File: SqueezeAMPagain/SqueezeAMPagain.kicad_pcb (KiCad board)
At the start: 2 copper layers, 100.5 x 104 mm, 183 parts, among them J1 Conn_01x02_Pin, J10 Conn_02x07_Odd_Even, J2 Conn_01x02_Pin, J3 Raspberry_Pi_2_3, J4 Conn_01x06_Pin, J5 USB_B_Micro, J6 Conn_01x02_Pin, J7 Barrel_Jack_Switch_MountingPin, J8 Conn_02x08_Odd_Even, J9 Conn_01x06_Pin, Q1 Q_NPN_BEC, Q10 AO3401A, Q3 AO3401A, Q4 Q_NPN_BEC, Q5 Q_NPN_BEC, Q6 Q_NPN_BEC, Q7 AO3401A, Q8 AO3401A, Q9 AO3401A, U1 TAS5756M, U2 RaspberryPi_Pico_W, U3 CP2102N-Axx-xQFN28, U4 ESP32-WROVER-E, U5 TPS5430DDA, U6 TSOP21xx, U7 AMS1117-3.3

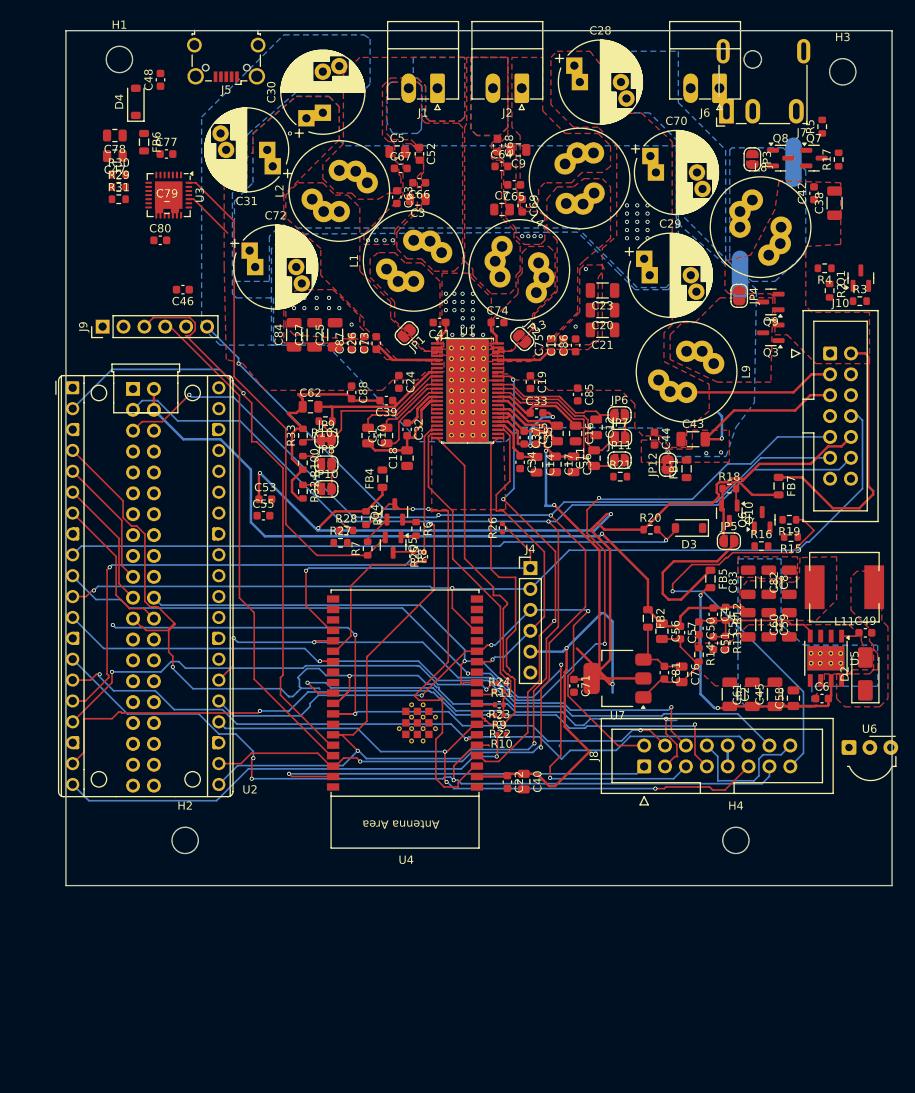
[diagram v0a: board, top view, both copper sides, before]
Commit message: Update SqueezeAMPagain.kicad_pcb, SqueezeAMPagain.kicad_prl, SqueezeAMPagain.kicad_pro, and 5 more files
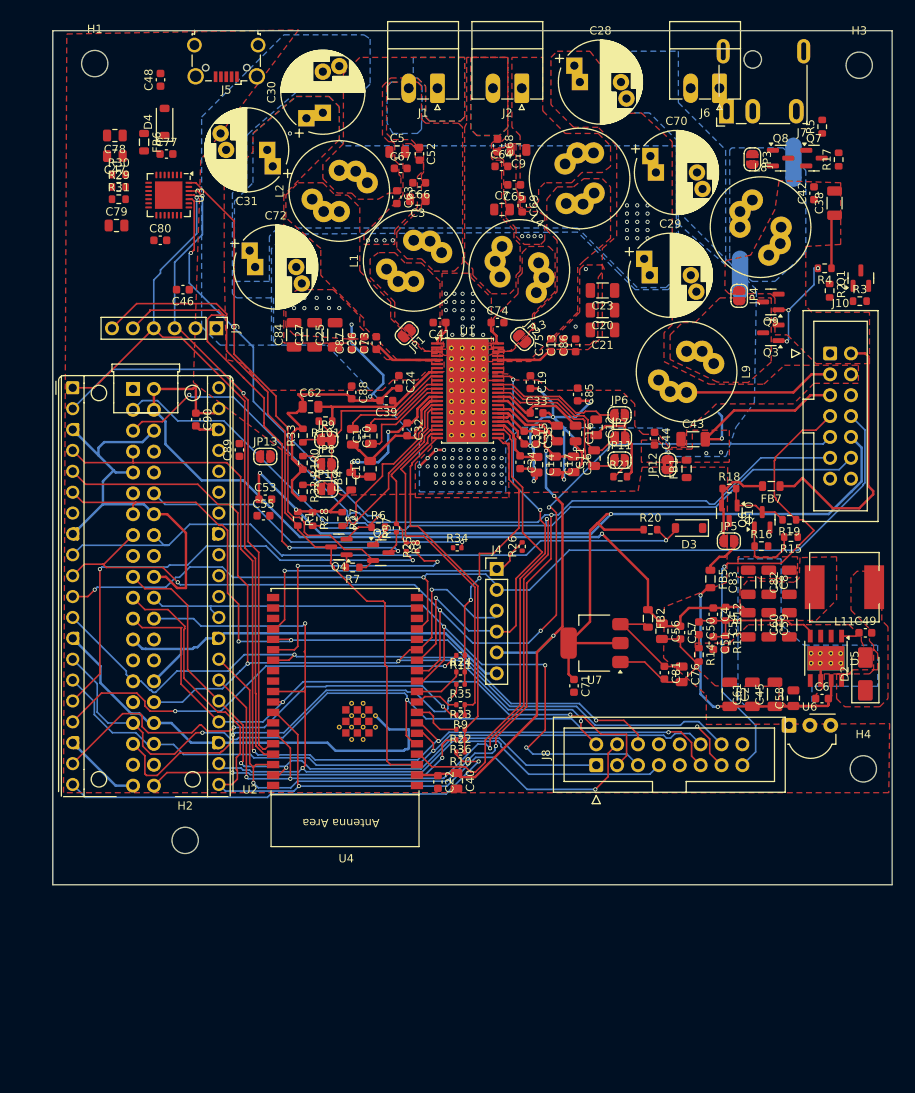
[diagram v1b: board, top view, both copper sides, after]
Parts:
- added C89: 100n, Capacitor_SMD:C_0603_1608Metric, F.Cu at (85.1, 71.0)
- added C90: 100n, Capacitor_SMD:C_0603_1608Metric, F.Cu at (79.8, 67.3)
- added JP13: LV On, Jumper:SolderJumper-2_P1.3mm_Open_RoundedPad1.0x1.5mm, F.Cu at (88.2, 71.8)
- added R34: 33, Resistor_SMD:R_0402_1005Metric, F.Cu at (111.6, 82.9)
- added R35: 33, Resistor_SMD:R_0402_1005Metric, F.Cu at (112.0, 99.5)
- added R36: 33, Resistor_SMD:R_0402_1005Metric, F.Cu at (112.0, 106.2)
- added R37: 33, Resistor_SMD:R_0402_1005Metric, F.Cu at (104.2, 80.5)
- U2: footprint pipico:RaspberryPi_Pico_Common_THT -> pipico_reduced:RaspberryPi_Pico_Common_THT_nokeepout
- moved H4 17.8 mm to (161.0, 109.8)
- moved J9 13.8 mm to (82.3, 56.2), turned to -90 degrees
- moved C22 8.45 mm to (109.2, 111.4)
- moved R1 8.30 mm to (92.2, 79.4)
- moved C40 8.20 mm to (111.5, 111.2)
- moved Q4 8.03 mm to (97.2, 82.8), turned to 180 degrees
- moved U6 7.78 mm to (152.0, 104.5)
- moved U4 7.30 mm to (98.0, 103.6)
- moved C79 6.53 mm to (70.2, 43.7)
- moved R11 6.05 mm to (112.0, 96.0)
- moved J8 5.83 mm to (128.5, 109.4)
- moved R10 5.44 mm to (112.0, 107.8)
- moved R24 5.29 mm to (112.0, 98.0)
- moved U7 5.13 mm to (128.3, 94.5)
- moved R22 4.84 mm to (112.0, 105.0)
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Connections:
- D3 pad 2: /Pico/GPIO6 -> /Pi/GPIO23
- J10 pad 9: /Pico/GPIO7 -> /Pi/GPIO22
- J3 pad 12: /Amp/SCLK -> Net-(J3-GPIO18/PWM0)
- J3 pad 13: unconnected-(J3-GPIO27-Pad13) -> /FPConnector/RESET
- J3 pad 15: unconnected-(J3-GPIO22-Pad15) -> /Pi/GPIO22
- J3 pad 16: unconnected-(J3-GPIO23-Pad16) -> /Pi/GPIO23
- J3 pad 18: unconnected-(J3-GPIO24-Pad18) -> /esp/TCK
- J3 pad 29: unconnected-(J3-GCLK1/GPIO5-Pad29) -> /FPConnector/IO4
- J3 pad 32: /Pi/PWM -> /esp/TDI
- J3 pad 33: unconnected-(J3-PWM1/GPIO13-Pad33) -> /FPConnector/IO3
- J3 pad 35: /Amp/LRCLK/FS -> Net-(J3-GPIO19/MISO1)
- J3 pad 36: unconnected-(J3-GPIO16-Pad36) -> /FPConnector/IO2
- J3 pad 40: /Amp/SDIN -> Net-(J3-GPIO21/SCLK1)
- J3 pad 7: unconnected-(J3-GCLK0/GPIO4-Pad7) -> /FPConnector/IO1
- R2 pad 1: /Pico/GPIO7 -> /Pi/GPIO22
- R20 pad 2: /Pico/GPIO6 -> /Pi/GPIO23
- R25 pad 2: /USB-Uart/BOOT -> /Amp/MCLK
- R26 pad 1: /Pico/GPIO6 -> /Pi/GPIO23
- R8 pad 1: /USB-Uart/BOOT -> /Amp/MCLK
- U1 pad 22: /USB-Uart/BOOT -> /Amp/MCLK
- U2 pad 10: /Pico/GPIO7 -> /Pi/GPIO22
- U2 pad 21: /SDA -> /FPConnector/MISO
- U2 pad 22: /SCL -> /FPConnector/CS
- U2 pad 24: /FPConnector/IO1 -> /FPConnector/SCK
- U2 pad 25: /esp/TDI -> /FPConnector/MOSI
- U2 pad 26: /FPConnector/RESET -> /SDA
- U2 pad 27: unconnected-(U2-GPIO21-Pad27) -> /SCL
- U2 pad 29: unconnected-(U2-GPIO22-Pad29) -> /FPConnector/D/C
- U2 pad 36: unconnected-(U2-3V3-Pad36) -> Net-(JP13-A)
- U2 pad 39: unconnected-(U2-VSYS-Pad39) -> +5V
- U2 pad 4: /FPConnector/SCK -> /FPConnector/IO1
- U2 pad 5: /FPConnector/MOSI -> /esp/TDI
- U2 pad 6: /FPConnector/MISO -> /FPConnector/RESET
- U2 pad 7: /FPConnector/CS -> unconnected-(U2-GPIO5-Pad7)
- U2 pad 9: /Pico/GPIO6 -> /Pi/GPIO23
- U4 pad 12: /Pico/GPIO7 -> /Pi/GPIO22
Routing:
- net GND: track 31.9 -> 191.5 mm
- net /Pi/GPIO22: track 0.00 -> 130.7 mm, vias 0 -> 4
- net /Pico/GPIO7: track 125.2 -> 0.00 mm, vias 3 -> 0
- net /Pi/GPIO23: track 0.00 -> 82.1 mm, vias 0 -> 1
- net /Pico/GPIO6: track 76.6 -> 0.00 mm, vias 1 -> 0
- net PGND: track 84.9 -> 156.7 mm, vias 46 -> 99
- net Net-(Q4-E): track 8.19 -> 60.1 mm, vias 0 -> 3
- net Net-(J3-GPIO19/MISO1): track 0.00 -> 50.5 mm, vias 0 -> 2
- net /esp/TDI: track 74.4 -> 123.3 mm, vias 3 -> 4
- net /FPConnector/SCK: track 123.7 -> 79.5 mm, vias 3 -> 2
- net /USB-Uart/BOOT: track 19.9 -> 64.0 mm, vias 0 -> 2
- net /FPConnector/IO1: track 76.6 -> 119.5 mm
- net Net-(J3-GPIO18/PWM0): track 0.00 -> 40.7 mm, vias 0 -> 1
- net Net-(J3-GPIO21/SCLK1): track 0.00 -> 40.3 mm, vias 0 -> 2
- net /SCL: track 170.2 -> 201.2 mm, vias 6 -> 5
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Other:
- board size 100.5 x 104 mm -> 102.1 x 103.9 mm

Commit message: Update SqueezeAMPagain.kicad_pcb, SqueezeAMPagain.kicad_prl, SqueezeAMPagain.kicad_pro, and 5 more files
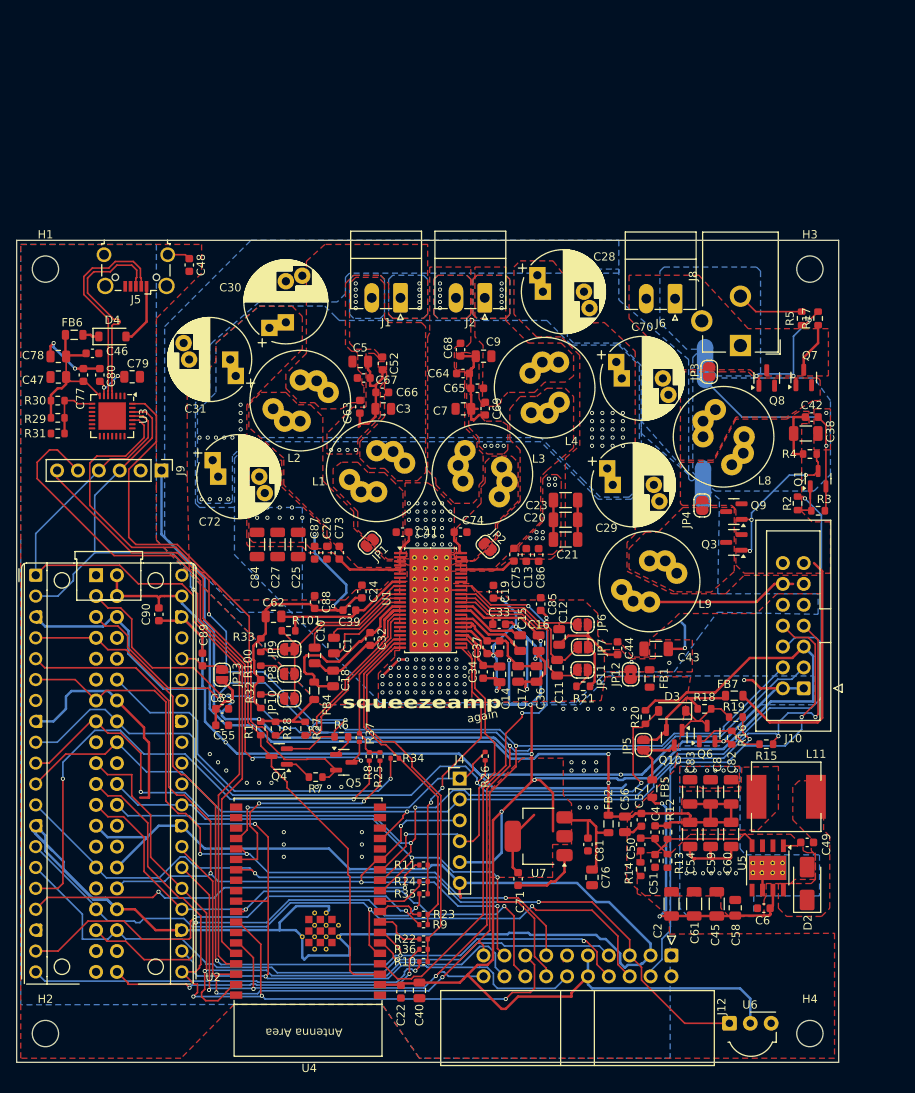
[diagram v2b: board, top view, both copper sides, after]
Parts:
- removed J7: Barrel_Jack_Switch_MountingPin, Connector_BarrelJack:BarrelJack_CUI_PJ-079BH_Horizontal
- added J12: Conn_02x10_Odd_Even, Connector_IDC:IDC-Header_2x10_P2.54mm_Horizontal, F.Cu at (137.7, 132.5)
- J8: value Conn_02x08_Odd_Even -> Barrel_Jack_Switch; footprint Connector_IDC:IDC-Header_2x08_P2.54mm_Vertical -> Connector_BarrelJack:BarrelJack_CUI_PJ-102AH_Horizontal
- moved J8 54.0 mm to (146.1, 58.3), turned to 180 degrees
- moved J10 40.9 mm to (153.8, 100.0), turned to 180 degrees
- moved U6 37.0 mm to (144.7, 140.8)
- moved H4 32.8 mm to (154.5, 142.0)
- moved R31 29.5 mm to (63.0, 69.0)
- moved R29 29.1 mm to (63.0, 67.1)
- moved H2 29.0 mm to (61.5, 142.0)
- moved C77 28.7 mm to (66.1, 61.9), turned to 90 degrees
- moved R30 28.5 mm to (63.0, 65.0)
- moved C38 28.2 mm to (154.0, 69.0), turned to 0 degrees
- moved Q10 28.1 mm to (138.0, 106.0)
- moved J5 27.8 mm to (72.5, 49.2)
- moved C47 27.7 mm to (63.1, 62.1)
- moved C78 27.7 mm to (63.1, 59.6)
- moved U3 27.7 mm to (69.6, 66.9)
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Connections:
- J10 pad 1: V_{IN} -> GND
- J10 pad 10: +3.3V -> PGND
- J10 pad 11: /SCL -> PVDD
- J10 pad 12: /SDA -> PVDD
- J10 pad 13: GND -> V_{IN}
- J10 pad 14: GND -> V_{IN}
- J10 pad 2: V_{IN} -> GND
- J10 pad 3: PVDD -> /SDA
- J10 pad 4: PVDD -> /SCL
- J10 pad 5: PGND -> +3.3V
- J10 pad 6: PGND -> /Pi/GPIO22
- J10 pad 7: /FPConnector/~{WAKE} -> /esp/TCK
- J10 pad 8: /esp/TCK -> /FPConnector/~{WAKE}
- J10 pad 9: /Pi/GPIO22 -> PGND
- J3 pad 17: Net-(J3-3V3-Pad1) -> pipin17
- J5 pad 6: Net-(J5-Shield) -> 6nc1
- J6 pad 1: Net-(J6-Pin_1) -> /Power/GND_{supply}
- J6 pad 2: /Power/V_{supply} -> /Power/V_{supply,plug}
- J8 pad 1: /FPConnector/MOSI -> /Power/V_{supply,plug}
- J8 pad 2: /esp/TDI -> /Power/GND_{supply}
- J8 pad 3: /FPConnector/SCK -> unconnected-(J8-Pad3)
- JP3 pad 1: /Power/V_{supply} -> /Power/V_{supply,plug}
- JP3 pad 2: Net-(JP3-B) -> /Power/V_{supply}
- L8 pad 1: Net-(JP3-B) -> /Power/V_{supply}
- NT1 pad 1: Net-(J6-Pin_1) -> /Power/GND_{supply}
- Q7 pad 2: Net-(JP3-B) -> /Power/V_{supply}
- Q7 pad 3: /Power/V_{supply} -> /Power/V_{supply,plug}
- Q8 pad 2: Net-(JP3-B) -> /Power/V_{supply}
- Q8 pad 3: /Power/V_{supply} -> /Power/V_{supply,plug}
- R17 pad 1: /Power/V_{supply} -> /Power/V_{supply,plug}
- R5 pad 2: Net-(J6-Pin_1) -> /Power/GND_{supply}
- U6 pad 1: unconnected-(U6-OUT-Pad1) -> /FPConnector/IO4
- U6 pad 3: unconnected-(U6-GND-Pad3) -> GND
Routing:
- net GND: track 191.5 -> 417.8 mm, vias 0 -> 49
- net +3.3V: track 219.4 -> 324.3 mm, vias 6 -> 8
- net /Power/GND_{IN}: track 0.00 -> 27.7 mm, vias 0 -> 2
- net /USB-Uart/D-: track 0.00 -> 26.0 mm
- net /USB-Uart/D+: track 0.00 -> 25.9 mm
- net /Pi/GPIO22: track 130.7 -> 153.4 mm
- net V_{USB}: track 0.00 -> 18.3 mm
- net Net-(Q7-G): track 0.00 -> 17.4 mm, vias 0 -> 3
- net /Pi/GPIO23: track 82.1 -> 98.7 mm, vias 1 -> 2
- net /FPConnector/D/C: track 86.8 -> 72.5 mm, vias 3 -> 2
- net Net-(Q4-E): track 60.1 -> 72.4 mm, vias 3 -> 2
- net +5V: track 103.4 -> 115.7 mm, vias 1 -> 2
- net /USB-Uart/BOOT: track 64.0 -> 75.2 mm
- net /FPConnector/IO3: track 101.6 -> 90.6 mm, vias 3 -> 2
- net /FPConnector/IO1: track 119.5 -> 109.6 mm
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- added copper zone on F.Cu, net +3.3V
- added copper zone on B.Cu, net /Amp/SPK_B+
- added copper zone on F.Cu, net /Power/GND_{IN}
- added copper zone on B.Cu, net /Power/GND_{supply}
- added copper zone on F.Cu, net /Power/V_{supply,plug}
- added copper zone on F.Cu, net /Power/V_{supply}
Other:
- board size 102.1 x 103.9 mm -> 100 x 100 mm
- board text added: "again"
- board text added: "squeezeamp"

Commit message: Update SqueezeAMPagain.kicad_pcb, SqueezeAMPagain.kicad_prl, SqueezeAMPagain.kicad_pro, and 11 more files
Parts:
- removed the C53 at (83.0, 102.5)
- J8: renamed from J5; footprint Connector_USB:USB_Micro-B_Wuerth_629105150521_CircularHoles -> Connector_USB:USB_Micro-B_XKB_U254-051T-4BH83-F1S
- moved J8 1.91 mm to (72.5, 47.3)
- renumbered C16 to C1, C15 to C10, C70 to C11, C32 to C12, C28 to C13, C29 to C14, C30 to C15, C31 to C16, C21 to C17, C19 to C18, C72 to C19, C36 to C2, C1 to C20, C20 to C21, C13 to C22, C10 to C23, C85 to C24, C23 to C25, C86 to C26, C11 to C27, C26 to C28, C25 to C29, C33 to C3, C12 to C30, C24 to C31, C27 to C32, C87 to C33, C39 to C34, C84 to C35, C88 to C36, C62 to C37, C41 to C38, C66 to C39, C37 to C4, C52 to C40, C3 to C41, C73 to C42, C67 to C43, C63 to C44, C5 to C45, C74 to C46, C68 to C47, C64 to C48, C7 to C49, C14 to C5, C75 to C50, C69 to C51, C65 to C52, C9 to C53, C22 to C54, C40 to C55, C55 to C56, C89 to C57, C90 to C58, C76 to C59, C34 to C6, C81 to C60, C2 to C62, C45 to C63, C71 to C64, C58 to C65, C38 to C66, C6 to C67, C42 to C68, C49 to C69, C17 to C7, C51 to C70, C50 to C71, C59 to C72, C4 to C73, C44 to C74, C60 to C75, C43 to C76, C54 to C77, C82 to C78, C8 to C79, C18 to C8, C57 to C80, C56 to C81, C83 to C82, C48 to C83, C46 to C84, C47 to C85, C78 to C86, C77 to C87, C80 to C88, C79 to C89, C35 to C9, D3 to D1, D4 to D3, FB4 to FB1, FB7 to FB2, FB2 to FB3, FB5 to FB4, FB1 to FB5, J4 to J3, J3 to J4, J12 to J5, J8 to J6, J6 to J7, JP10 to JP1, JP5 to JP10, JP3 to JP11, JP4 to JP12, JP12 to JP13, JP8 to JP2, JP9 to JP3, JP1 to JP4, JP11 to JP5, JP2 to JP6, JP6 to JP8, JP13 to JP9, L8 to L5, L11 to L6, L9 to L7, Q6 to Q1, Q10 to Q2, Q7 to Q3, Q8 to Q4, Q1 to Q5, Q3 to Q6, Q9 to Q7, Q4 to Q8, Q5 to Q9, R37 to R1, R22 to R10, R23 to R11, R1 to R12, R25 to R13, R24 to R14, R36 to R15, R34 to R16, R35 to R17, R8 to R18, R11 to R19, R27 to R2, R9 to R20, R10 to R21, R19 to R22, R15 to R23, R18 to R24, R16 to R25, R17 to R26, R5 to R27, R20 to R28, R2 to R29, R28 to R3, R4 to R30, R3 to R31, R14 to R32, R12 to R33, R13 to R34, R29 to R35, R30 to R36, R31 to R37, R6 to R38, R7 to R39, R32 to R4, R100 to R5, R101 to R6, R33 to R7, R21 to R8, R26 to R9, U4 to U2, U2 to U3, U6 to U4, U7 to U5, U5 to U6, U3 to U7
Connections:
- J4 pad 1: Net-(J3-3V3-Pad1) -> Net-(J4-3V3-Pad1)
- J4 pad 17: pipin17 -> Net-(J4-3V3-Pad1)
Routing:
- net /USB-Uart/D-: track 26.0 -> 18.5 mm, vias 0 -> 2
- net /USB-Uart/D+: track 25.9 -> 20.0 mm, vias 0 -> 2
- net Net-(J8-Shield): track 2.82 -> 6.18 mm
- net Net-(D3-A): track 7.55 -> 9.07 mm

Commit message: Update SqueezeAMPagain.kicad_pcb, SqueezeAMPagain.kicad_prl, SqueezeAMPagain.kicad_pro, and 4 more files
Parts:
- added C90: 2.2u/25V, Capacitor_SMD:C_0805_2012Metric, F.Cu at (126.8, 102.0)
- added C91: 100n, Capacitor_SMD:C_0603_1608Metric, F.Cu at (122.8, 102.5)
- added H5: MountingHole, MountingHole:MountingHole_2.5mm, F.Cu at (108.1, 80.1)
- added Q10: AO3401A, Package_TO_SOT_SMD:SOT-23, F.Cu at (121.5, 105.4)
- added Q11: Q_NPN_BEC, Package_TO_SOT_SMD:SOT-23, F.Cu at (125.7, 105.0)
- added R40: 150k, Resistor_SMD:R_0603_1608Metric, F.Cu at (121.8, 109.8)
- added R41: 10k, Resistor_SMD:R_0603_1608Metric, F.Cu at (124.2, 109.8)
- added R42: 10k, Resistor_SMD:R_0603_1608Metric, F.Cu at (128.8, 105.1)
- D2: value SS34 550mV 2A -> SS34 550mV 2A
- moved R3 27.5 mm to (117.0, 105.5)
- moved R2 25.6 mm to (118.7, 105.5)
- moved J10 15.4 mm to (151.3, 84.8), turned to 0 degrees
- moved R28 8.90 mm to (134.5, 112.4), turned to 90 degrees
- moved R16 6.85 mm to (107.8, 114.2)
- moved R38 5.80 mm to (92.8, 109.3)
- moved R1 5.30 mm to (99.9, 111.3)
- moved R12 4.44 mm to (86.0, 109.0)
- moved U5 3.60 mm to (121.5, 121.6)
- moved R13 3.06 mm to (102.8, 111.3)
- moved R18 3.05 mm to (101.4, 111.3)
- moved C64 2.98 mm to (119.7, 126.1)
- moved Q8 2.55 mm to (88.8, 110.6)
- moved R39 1.86 mm to (92.7, 111.6)
- moved Q9 1.85 mm to (96.9, 110.6)
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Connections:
- C1 pad 1: +3.3V -> +3.3V_{SW}
- C2 pad 1: +3.3V -> +3.3V_{SW}
- C3 pad 1: +3.3V -> +3.3V_{SW}
- C4 pad 1: +3.3V -> +3.3V_{SW}
- C7 pad 1: +3.3V -> +3.3V_{SW}
- C9 pad 1: +3.3V -> +3.3V_{SW}
- J10 pad 1: GND -> V_{IN}
- J10 pad 10: PGND -> +3.3V
- J10 pad 11: PVDD -> /SCL
- J10 pad 12: PVDD -> /SDA
- J10 pad 13: V_{IN} -> GND
- J10 pad 14: V_{IN} -> GND
- J10 pad 2: GND -> V_{USB}
- J10 pad 3: /SDA -> PVDD
- J10 pad 4: /SCL -> PVDD
- J10 pad 5: +3.3V -> PGND
- J10 pad 6: /Pi/GPIO22 -> PGND
- J10 pad 7: /esp/TCK -> /FPConnector/~{WAKE}
- J10 pad 8: /FPConnector/~{WAKE} -> /esp/TCK
- J10 pad 9: PGND -> /Pi/GPIO22
- J8 pad 6: 6nc1 -> Net-(J8-Shield)
- U1 pad 30: +3.3V -> +3.3V_{SW}
- U1 pad 31: +3.3V -> +3.3V_{SW}
- U1 pad 35: +3.3V -> +3.3V_{SW}
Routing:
- net V_{USB}: track 18.3 -> 154.3 mm, vias 0 -> 1
- net GND: track 417.8 -> 310.2 mm, vias 49 -> 43
- net +3.3V_{SW}: track 0.00 -> 45.1 mm
- net +3.3V: track 324.3 -> 291.9 mm, vias 8 -> 6
- net +5V: track 115.7 -> 135.4 mm
- net /USB-Uart/EN/~{RESET}: track 82.7 -> 97.4 mm, vias 0 -> 2
- net /esp/TDO: track 35.8 -> 48.0 mm, vias 1 -> 2
- net /USB-Uart/BOOT: track 75.2 -> 86.4 mm
- net /Pi/GPIO23: track 98.7 -> 109.1 mm
- net /SDA: track 210.6 -> 219.3 mm, vias 7 -> 6
- net Net-(Q10-G): track 0.00 -> 7.88 mm
- net /FPConnector/CS: track 93.2 -> 85.9 mm
- net Net-(Q11-B): track 0.00 -> 7.19 mm
- net /Pi/GPIO22: track 153.4 -> 160.6 mm
- net Net-(U3-GPIO12): track 64.2 -> 69.9 mm
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- added copper zone on F.Cu, net +3.3V_{SW}
